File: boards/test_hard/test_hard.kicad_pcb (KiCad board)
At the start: 2 copper layers, 2 parts, among them IC1 ADS114S08BIPBS, U2 ESP32-S3-MINI-1

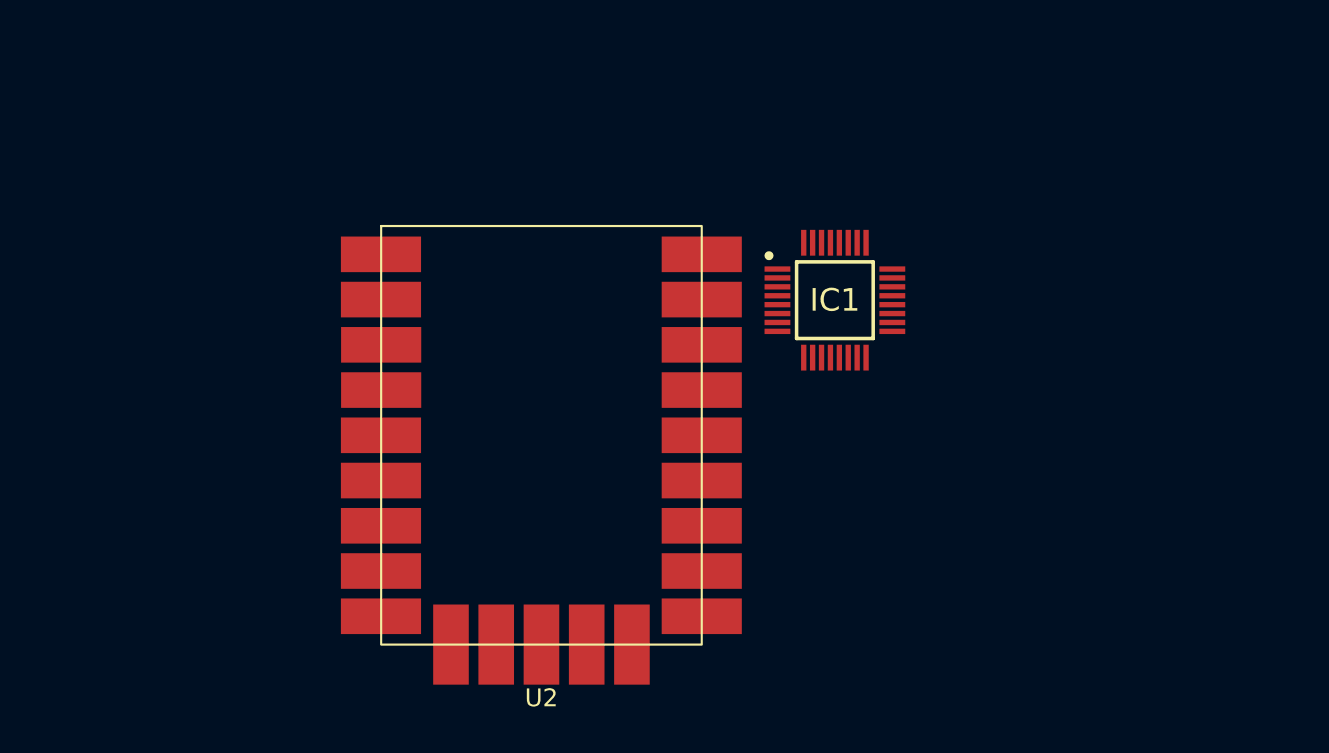
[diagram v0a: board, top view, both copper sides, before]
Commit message: Test Hardware Board
Still missing CAN

Signed-off-by: Philipp Macher <philipp-macher@web.de>
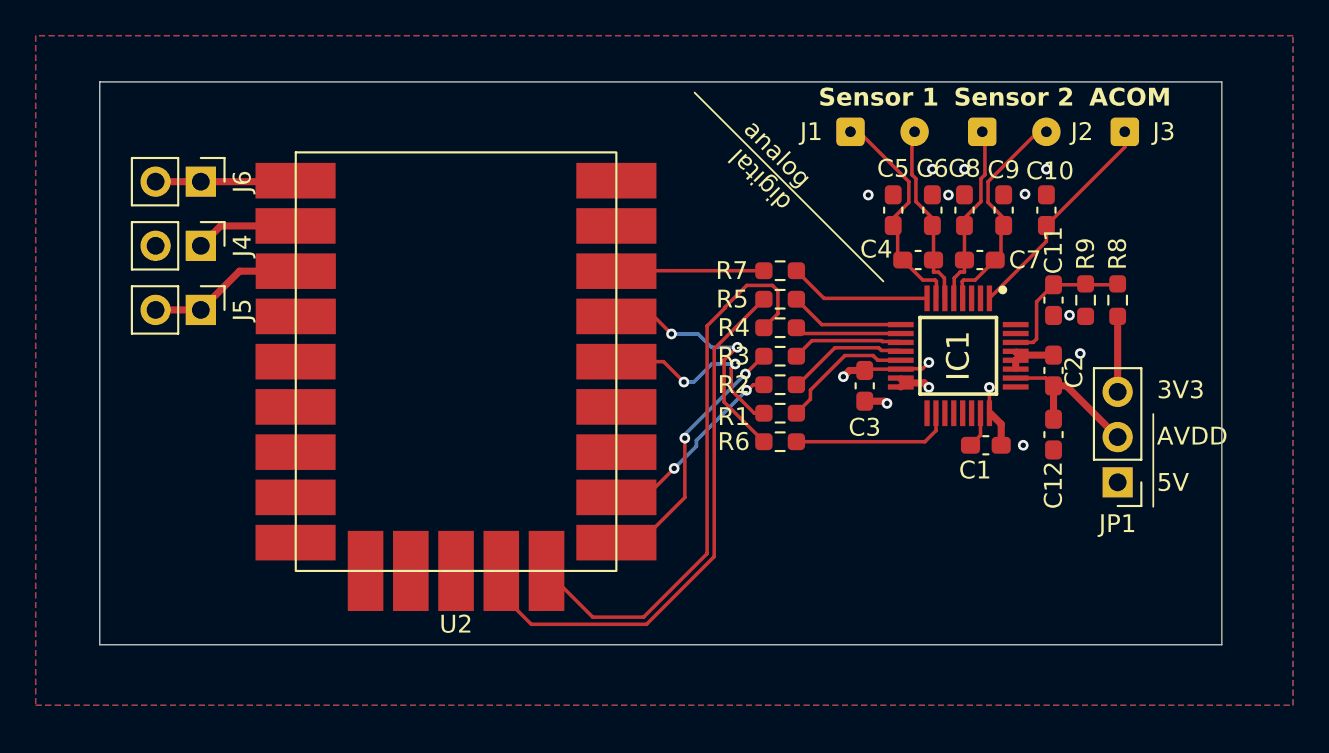
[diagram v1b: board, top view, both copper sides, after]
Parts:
- added C1: 1u, Capacitor_SMD:C_0603_1608Metric_Pad1.08x0.95mm_HandSolder, F.Cu at (143.9, 93.4)
- added C10: 470p, Capacitor_SMD:C_0603_1608Metric_Pad1.08x0.95mm_HandSolder, F.Cu at (147.3, 80.2)
- added C11: 4700p, Capacitor_SMD:C_0603_1608Metric_Pad1.08x0.95mm_HandSolder, F.Cu at (147.8, 85.2)
- added C12: 220n, Capacitor_SMD:C_0603_1608Metric_Pad1.08x0.95mm_HandSolder, F.Cu at (147.8, 92.8)
- added C2: 100n, Capacitor_SMD:C_0603_1608Metric_Pad1.08x0.95mm_HandSolder, F.Cu at (147.8, 89.2)
- added C3: 0,1u, Capacitor_SMD:C_0603_1608Metric_Pad1.08x0.95mm_HandSolder, F.Cu at (137.2, 90.1)
- added C4: 4700p, Capacitor_SMD:C_0603_1608Metric_Pad1.08x0.95mm_HandSolder, F.Cu at (140.2, 83.0)
- added C5: 470p, Capacitor_SMD:C_0603_1608Metric_Pad1.08x0.95mm_HandSolder, F.Cu at (138.8, 80.2)
- added C6: 470p, Capacitor_SMD:C_0603_1608Metric_Pad1.08x0.95mm_HandSolder, F.Cu at (140.9, 80.2)
- added C7: 4700p, Capacitor_SMD:C_0603_1608Metric_Pad1.08x0.95mm_HandSolder, F.Cu at (143.6, 83.0)
- added C8: 470p, Capacitor_SMD:C_0603_1608Metric_Pad1.08x0.95mm_HandSolder, F.Cu at (142.8, 80.2)
- added C9: 470p, Capacitor_SMD:C_0603_1608Metric_Pad1.08x0.95mm_HandSolder, F.Cu at (144.9, 80.2)
- added J1: Sensor 1, Connector_Wire:SolderWire-0.1sqmm_1x02_P3.6mm_D0.4mm_OD1mm, F.Cu at (136.3, 75.8)
- added J2: Sensor 2, Connector_Wire:SolderWire-0.1sqmm_1x02_P3.6mm_D0.4mm_OD1mm, F.Cu at (143.8, 75.8)
- added J3: ACOM, Connector_Wire:SolderWire-0.1sqmm_1x01_D0.4mm_OD1mm, F.Cu at (151.8, 75.8)
- added J4: GND, Connector_PinHeader_2.54mm:PinHeader_1x02_P2.54mm_Vertical, F.Cu at (99.9, 82.2)
- added J5: 3V3, Connector_PinHeader_2.54mm:PinHeader_1x02_P2.54mm_Vertical, F.Cu at (99.9, 85.8)
- added J6: 5V, Connector_PinHeader_2.54mm:PinHeader_1x02_P2.54mm_Vertical, F.Cu at (99.9, 78.6)
- added JP1: Jumper_3_Bridged12, Connector_PinHeader_2.54mm:PinHeader_1x03_P2.54mm_Vertical, F.Cu at (151.3, 95.5)
- added R1: 47, Resistor_SMD:R_0603_1608Metric_Pad0.98x0.95mm_HandSolder, F.Cu at (132.4, 91.6)
- added R2: 47, Resistor_SMD:R_0603_1608Metric_Pad0.98x0.95mm_HandSolder, F.Cu at (132.4, 90.0)
- added R3: 47, Resistor_SMD:R_0603_1608Metric_Pad0.98x0.95mm_HandSolder, F.Cu at (132.4, 88.4)
- added R4: 47, Resistor_SMD:R_0603_1608Metric_Pad0.98x0.95mm_HandSolder, F.Cu at (132.4, 86.8)
- added R5: 47, Resistor_SMD:R_0603_1608Metric_Pad0.98x0.95mm_HandSolder, F.Cu at (132.4, 85.2)
- added R6: 47, Resistor_SMD:R_0603_1608Metric_Pad0.98x0.95mm_HandSolder, F.Cu at (132.4, 93.2)
- added R7: 47, Resistor_SMD:R_0603_1608Metric_Pad0.98x0.95mm_HandSolder, F.Cu at (132.4, 83.6)
- added R8: 10k, Resistor_SMD:R_0603_1608Metric_Pad0.98x0.95mm_HandSolder, F.Cu at (151.3, 85.2)
- added R9: 10k, Resistor_SMD:R_0603_1608Metric_Pad0.98x0.95mm_HandSolder, F.Cu at (149.6, 85.2)
- moved IC1 7.60 mm to (142.4, 88.4), turned to -90 degrees
- moved U2 6.33 mm to (123.2, 98.9)
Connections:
- IC1 pad 1: unconnected-(IC1-AINCOM-Pad1) -> /ACOM
- IC1 pad 10: unconnected-(IC1-DIN-Pad10) -> Net-(IC1-DIN)
- IC1 pad 11: unconnected-(IC1-SCLK-Pad11) -> Net-(IC1-SCLK)
- IC1 pad 12: unconnected-(IC1-DOUT/~{DRDY}-Pad12) -> Net-(IC1-DOUT/~{DRDY})
- IC1 pad 13: unconnected-(IC1-~{DRDY}-Pad13) -> Net-(IC1-~{DRDY})
- IC1 pad 14: unconnected-(IC1-DGND-Pad14) -> GND
- IC1 pad 15: unconnected-(IC1-IOVDD-Pad15) -> +3V3
- IC1 pad 16: unconnected-(IC1-DVDD-Pad16) -> +3V3
- IC1 pad 18: unconnected-(IC1-~{RESET}-Pad18) -> Net-(IC1-~{RESET})
- IC1 pad 2: unconnected-(IC1-AIN5-Pad2) -> /GP2
- IC1 pad 23: unconnected-(IC1-REFOUT-Pad23) -> /REFOUT
- IC1 pad 24: unconnected-(IC1-REFCOM-Pad24) -> GND
- IC1 pad 26: unconnected-(IC1-AVDD-Pad26) -> /AVDD
- IC1 pad 27: unconnected-(IC1-AVSS_1-Pad27) -> GND
- IC1 pad 28: unconnected-(IC1-AVSS_2-Pad28) -> GND
- IC1 pad 29: unconnected-(IC1-REFN0-Pad29) -> GND
- IC1 pad 3: unconnected-(IC1-AIN4-Pad3) -> /GP1
- IC1 pad 30: unconnected-(IC1-REFP0-Pad30) -> /REFP
- IC1 pad 4: unconnected-(IC1-AIN3-Pad4) -> /D2P
- IC1 pad 5: unconnected-(IC1-AIN2-Pad5) -> /D2N
- IC1 pad 6: unconnected-(IC1-AIN1-Pad6) -> /D1P
- IC1 pad 7: unconnected-(IC1-AIN0-Pad7) -> /D1N
- IC1 pad 8: unconnected-(IC1-START/SYNC-Pad8) -> Net-(IC1-START/SYNC)
- IC1 pad 9: unconnected-(IC1-~{CS}-Pad9) -> Net-(IC1-~{CS})
- U2 pad 1: unconnected-(U2-5V-Pad1) -> +5V
- U2 pad 13: unconnected-(U2-IO10-Pad13) -> /CS
- U2 pad 14: unconnected-(U2-IO11-Pad14) -> /MOSI
- U2 pad 15: unconnected-(U2-IO12-Pad15) -> /CLK
- U2 pad 16: unconnected-(U2-IO13-Pad16) -> /MISO
- U2 pad 19: unconnected-(U2-IO16-Pad19) -> /DRDY
- U2 pad 2: Net-(U2-GND-Pad2) -> GND
- U2 pad 20: unconnected-(U2-IO17-Pad20) -> /C_RES
- U2 pad 21: unconnected-(U2-IO18-Pad21) -> /START
- U2 pad 3: unconnected-(U2-3V3-Pad3) -> +3V3
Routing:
- net /MOSI: track 0.00 -> 31.8 mm
- net /CS: track 0.00 -> 31.1 mm
- net GND: track 0.00 -> 17.4 mm, vias 0 -> 12
- net +3V3: track 0.00 -> 15.8 mm, vias 0 -> 2
- net /CLK: track 0.00 -> 14.7 mm, vias 0 -> 2
- net /C_RES: track 0.00 -> 14.1 mm, vias 0 -> 2
- net /ACOM: track 0.00 -> 12.5 mm
- net /DRDY: track 0.00 -> 11.5 mm, vias 0 -> 2
- net /D2P: track 0.00 -> 11.1 mm
- net /MISO: track 0.00 -> 11.1 mm, vias 0 -> 2
- net /D1N: track 0.00 -> 11.1 mm
- net /D2N: track 0.00 -> 9.61 mm
- net /D1P: track 0.00 -> 9.58 mm
- net Net-(IC1-~{RESET}): track 0.00 -> 9.07 mm
- net /AVDD: track 0.00 -> 8.97 mm
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- added copper zone on In2.Cu, net +3V3
- added copper zone on B.Cu, net +5V
- added copper zone on F.Cu, net GND
- added copper zone on In1.Cu, net GND
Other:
- board outline added: 63 x 31.6 mm
- copper layers 2 -> 4
- board text added: "3V3"
- board text added: "5V"
- board text added: "ACOM"
- board text added: "AVDD"
- board text added: "Sensor 1"
- board text added: "Sensor 2"
- board text added: "analog"
- board text added: "digital"

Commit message: Add CAN support to test hardware
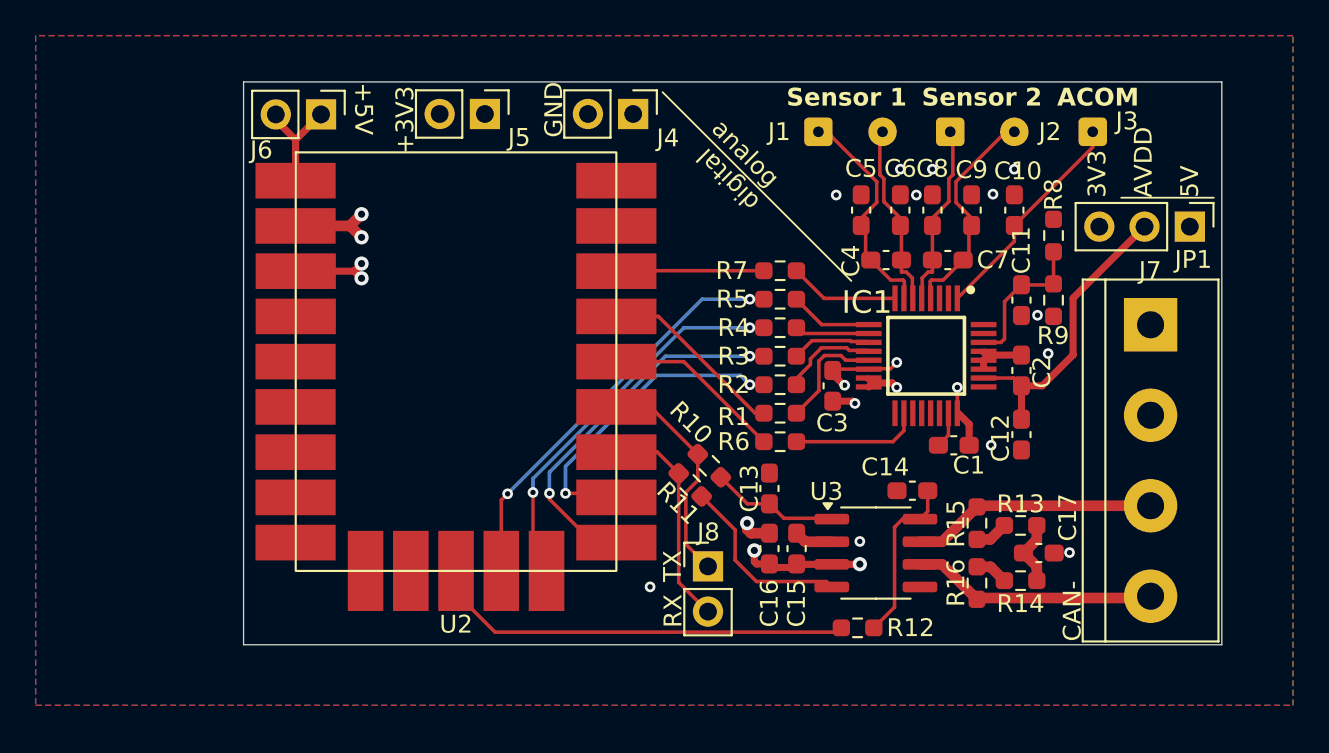
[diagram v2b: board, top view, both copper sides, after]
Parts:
- added C13: 100n, Capacitor_SMD:C_0603_1608Metric_Pad1.08x0.95mm_HandSolder, F.Cu at (131.8, 95.8)
- added C14: 100n, Capacitor_SMD:C_0603_1608Metric_Pad1.08x0.95mm_HandSolder, F.Cu at (139.8, 96.0)
- added C15: 100n, Capacitor_SMD:C_0603_1608Metric_Pad1.08x0.95mm_HandSolder, F.Cu at (133.3, 99.2)
- added C16: 22u, Capacitor_SMD:C_0603_1608Metric_Pad1.08x0.95mm_HandSolder, F.Cu at (131.8, 99.2)
- added C17: 4,7n, Capacitor_SMD:C_0603_1608Metric_Pad1.08x0.95mm_HandSolder, F.Cu at (146.9, 99.5)
- added J7: Conn_01x04, TerminalBlock:TerminalBlock_bornier-4_P5.08mm, F.Cu at (153.2, 86.6)
- added J8: Conn_01x02, Connector_PinHeader_2.54mm:PinHeader_1x02_P2.54mm_Vertical, F.Cu at (128.3, 100.2)
- added R10: 0, Resistor_SMD:R_0603_1608Metric_Pad0.98x0.95mm_HandSolder, F.Cu at (128.4, 94.5)
- added R11: 0, Resistor_SMD:R_0603_1608Metric_Pad0.98x0.95mm_HandSolder, F.Cu at (127.3, 95.6)
- added R12: 0/10k-100k, Resistor_SMD:R_0603_1608Metric_Pad0.98x0.95mm_HandSolder, F.Cu at (136.8, 103.7)
- added R13: 47, Resistor_SMD:R_0603_1608Metric_Pad0.98x0.95mm_HandSolder, F.Cu at (145.9, 97.9)
- added R14: 47, Resistor_SMD:R_0603_1608Metric_Pad0.98x0.95mm_HandSolder, F.Cu at (145.9, 101.0)
- added R15: 13, Resistor_SMD:R_0603_1608Metric_Pad0.98x0.95mm_HandSolder, F.Cu at (143.4, 97.8)
- added R16: 13, Resistor_SMD:R_0603_1608Metric_Pad0.98x0.95mm_HandSolder, F.Cu at (143.4, 101.1)
- added U3: SN65HVD230, Package_SO:SOIC-8_3.9x4.9mm_P1.27mm, F.Cu at (137.8, 99.5)
- moved J4 25.4 mm to (124.2, 74.8)
- moved J5 19.4 mm to (115.8, 74.8)
- moved JP1 14.9 mm to (155.4, 81.1), turned to -90 degrees
- moved J6 7.73 mm to (106.6, 74.8)
- moved R8 5.11 mm to (147.8, 81.6), turned to -90 degrees
- moved C11 1.80 mm to (145.9, 85.2)
- moved C12 1.80 mm to (145.9, 92.8)
- moved C2 1.80 mm to (145.9, 89.2)
- moved C3 1.80 mm to (135.3, 90.1)
- moved C4 1.80 mm to (138.3, 83.0)
- moved C5 1.80 mm to (136.9, 80.2)
- moved C7 1.80 mm to (141.8, 83.0)
- moved C8 1.80 mm to (140.9, 80.2)
- moved IC1 1.80 mm to (140.6, 88.4)
- moved J2 1.80 mm to (141.9, 75.8)
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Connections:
- net /ACOM renamed /ADC/ACOM
- net /AVDD renamed /ADC/AVDD
- net /CLK renamed /ADC/SPI.CLK
- net /CS renamed /ADC/SPI.CS
- net /D1N renamed /ADC/D1N
- net /D1P renamed /ADC/D1P
- net /D2N renamed /ADC/D2N
- net /D2P renamed /ADC/D2P
- net /GP1 renamed /ADC/GP1
- net /GP2 renamed /ADC/GP2
- net /MISO renamed /ADC/SPI.MISO
- net /MOSI renamed /ADC/SPI.MOSI
- net /REFOUT renamed /ADC/REFOUT
- net /REFP renamed /ADC/REFP
- U2 pad 12: unconnected-(U2-IO9-Pad12) -> /Rs
- U2 pad 17: unconnected-(U2-IO14-Pad17) -> /CAN_RX
- U2 pad 18: unconnected-(U2-IO15-Pad18) -> /CAN_TX
- U2 pad 19: /DRDY -> /C_RES
- U2 pad 20: /C_RES -> /DRDY
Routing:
- net /Rs: track 0.00 -> 23.9 mm
- net /CAN+: track 0.00 -> 13.8 mm
- net /CAN-: track 0.00 -> 13.4 mm
- net /CAN_TX: track 0.00 -> 12.8 mm
- net /CAN_RX: track 0.00 -> 12.4 mm
- net /ADC/SPI.MOSI: track 31.8 -> 20.9 mm, vias 0 -> 2
- net Net-(U3-R): track 0.00 -> 10.4 mm
- net Net-(U3-Rs): track 0.00 -> 9.52 mm
- net /ADC/SPI.CS: track 31.1 -> 23.4 mm, vias 0 -> 2
- net /ADC/AVDD: track 8.97 -> 16.7 mm
- net Net-(U3-D): track 0.00 -> 7.20 mm
- net /ADC/SPI.MISO: track 11.1 -> 17.9 mm
- net /ADC/SPI.CLK: track 14.7 -> 19.7 mm
- net /C_RES: track 14.1 -> 10.1 mm, vias 2 -> 0
- net Net-(C17-Pad1): track 0.00 -> 3.72 mm
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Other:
- board size 63 x 31.6 mm -> 54.9 x 31.6 mm
- board text added: "+3V3"
- board text added: "+5V"
- board text added: "CAN+"
- board text added: "CAN-"
- board text added: "GND"
- board text added: "RX"
- board text added: "TX"

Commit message: 1Ohm res and stencil
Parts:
- added R17: 1, Resistor_SMD:R_0603_1608Metric_Pad0.98x0.95mm_HandSolder, F.Cu at (137.2, 77.8)
- added R18: 1, Resistor_SMD:R_0603_1608Metric_Pad0.98x0.95mm_HandSolder, F.Cu at (142.9, 77.8)
- moved C10 0.26 mm to (145.6, 80.5)
- moved C5 0.26 mm to (136.9, 80.5)
- moved C6 0.26 mm to (139.2, 80.5)
- moved C8 0.26 mm to (140.9, 80.5)
- moved C9 0.26 mm to (143.2, 80.5)
- moved J1 0.12 mm to (134.6, 75.7)
- moved J2 0.12 mm to (141.9, 75.7)
- moved J3 0.12 mm to (149.9, 75.7)
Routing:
- net /ADC/ACOM: track 12.5 -> 0.00 mm
- net /CAN_TX: track 12.8 -> 10.8 mm
- net /ADC/D1N: track 11.1 -> 12.9 mm
- net /Rs: track 23.9 -> 22.3 mm
- net /ADC/D2P: track 11.1 -> 12.5 mm
- net /ADC/D1P: track 9.58 -> 10.3 mm
- net /ADC/D2N: track 9.61 -> 10.2 mm

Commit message: Fabricated
Signed-off-by: Philipp Macher <philipp-macher@web.de>
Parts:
- moved R12 0.30 mm to (136.8, 103.3)
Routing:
- net /ADC/ACOM: track 0.00 -> 12.6 mm
- net +3V3: track 14.3 -> 17.0 mm
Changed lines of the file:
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@@
 	(footprint "Resistor_SMD:R_0603_1608Metric_Pad0.98x0.95mm_HandSolder"
 		(layer "F.Cu")
-		(at 136.75 103.65)
+		(at 136.75 103.35)
 		(descr "Resistor SMD 0603 (1608 Metric), square (rectangular) end terminal, IPC_7351 nominal with elongated pad for handsoldering. (Body size source: IPC-SM-782 page 72, https://www.pcb-3d.com/wordpress/wp-content/uploads/ipc-sm-782a_amendment_1_and_2.pdf), generated with kicad-footprint-generator")
 		(tags "resistor handsolder")
@@
 		(layer "F.SilkS")
 	)
+	(gr_rect
+		(start 104.6 97.8)
+		(end 109.6 102.8)
+		(stroke
+			(width 0.1)
+			(type solid)
+		)
+		(fill yes)
+		(layer "B.SilkS")
+	)
 	(gr_line
 		(start 102.275 73)
@@
 	)
 	(via
-		(at 139.15 78.75)
+		(at 139.2 78.3)
 		(size 0.6)
 		(drill 0.3)
@@
 	)
 	(via
-		(at 140.95 78.75)
+		(at 140.8 78.45)
 		(size 0.6)
 		(drill 0.3)
@@
 	)
 	(segment
+		(start 149.9075 80.7125)
+		(end 150.32 81.125)
+		(width 0.4)
+		(layer "F.Cu")
+		(net 5)
+	)
+	(segment
 		(start 108.475 83.625)
 		(end 108.875 84.025)
@@
 	)
 	(segment
+		(start 147.75 80.7125)
+		(end 149.9075 80.7125)
+		(width 0.4)
+		(layer "F.Cu")
+		(net 5)
+	)
+	(segment
 		(start 131.8 100.2625)
 		(end 133.325 100.2625)
@@
 	)
 	(segment
+		(start 149.95 76.925)
+		(end 149.95 75.675)
+		(width 0.2)
+		(layer "F.Cu")
+		(net 17)
+	)
+	(segment
+		(start 145.55 81.325)
+		(end 149.95 76.925)
+		(width 0.2)
+		(layer "F.Cu")
+		(net 17)
+	)
+	(segment
+		(start 142.35 85.15)
+		(end 145.55 81.95)
+		(width 0.2)
+		(layer "F.Cu")
+		(net 17)
+	)
+	(segment
+		(start 145.55 81.95)
+		(end 145.55 81.325)
+		(width 0.2)
+		(layer "F.Cu")
+		(net 17)
+	)
+	(segment
 		(start 134.8625 85.15)
 		(end 133.3125 83.6)
@@
 	)
 	(segment
-		(start 138.825 102.4875)
-		(end 137.6625 103.65)
+		(start 138.825 97.995001)
+		(end 138.825 102.1875)
 		(width 0.2)
 		(layer "F.Cu")
@@
 	)
 	(segment
-		(start 140.25 97.545)
-		(end 139.275001 97.545)
+		(start 138.825 102.1875)
+		(end 137.6625 103.35)
 		(width 0.2)
 		(layer "F.Cu")
@@
 	)
 	(segment
-		(start 140.6875 95.95)
-		(end 140.6875 97.1075)
+		(start 140.25 97.545)
+		(end 139.275001 97.545)
 		(width 0.2)
 		(layer "F.Cu")
@@
 	)
 	(segment
-		(start 138.825 97.995001)
-		(end 138.825 102.4875)
+		(start 140.6875 95.95)
+		(end 140.6875 97.1075)
 		(width 0.2)
 		(layer "F.Cu")
@@
 	)
 	(segment
-		(start 116.391 103.891)
+		(start 127.87324 103.891)
+		(end 127.33224 103.35)
+		(width 0.2)
+		(layer "F.Cu")
+		(net 47)
+	)
+	(segment
+		(start 127.33224 103.35)
+		(end 115.85 103.35)
+		(width 0.2)
+		(layer "F.Cu")
+		(net 47)
+	)
+	(segment
+		(start 115.85 103.35)
 		(end 114.205 101.705)
 		(width 0.2)
@@
 	)
 	(segment
-		(start 135.5965 103.891)
-		(end 116.391 103.891)
+		(start 135.8375 103.35)
+		(end 129.36776 103.35)
+		(width 0.2)
+		(layer "F.Cu")
+		(net 47)
+	)
+	(segment
+		(start 129.36776 103.35)
+		(end 128.82676 103.891)
+		(width 0.2)
+		(layer "F.Cu")
+		(net 47)
+	)
+	(segment
+		(start 128.82676 103.891)
+		(end 127.87324 103.891)
 		(width 0.2)
 		(layer "F.Cu")
